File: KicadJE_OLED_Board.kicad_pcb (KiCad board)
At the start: 2 copper layers, 170.6 x 128 mm, 164 parts, among them J1 LED 1-6, J201 OLED, J202 ADC Input, J203 Out2, J204 Out1, J205 OUT1, J206 OUT2, J207 IN1, J208 IN2, J209 CV1, J210 CV2, J211 FrontLED, J212 -12V Front, J301 UART, J302 AVR-ISP-6, P1 Doepfer_Power_16pin, P201 Doepfer_Power_16pin, SW201 Rotary_Encoder_Switch, SW202 Rotary_Encoder_Switch, U201 TL072, U301 ATmega32A-AU, Y301 16MHz

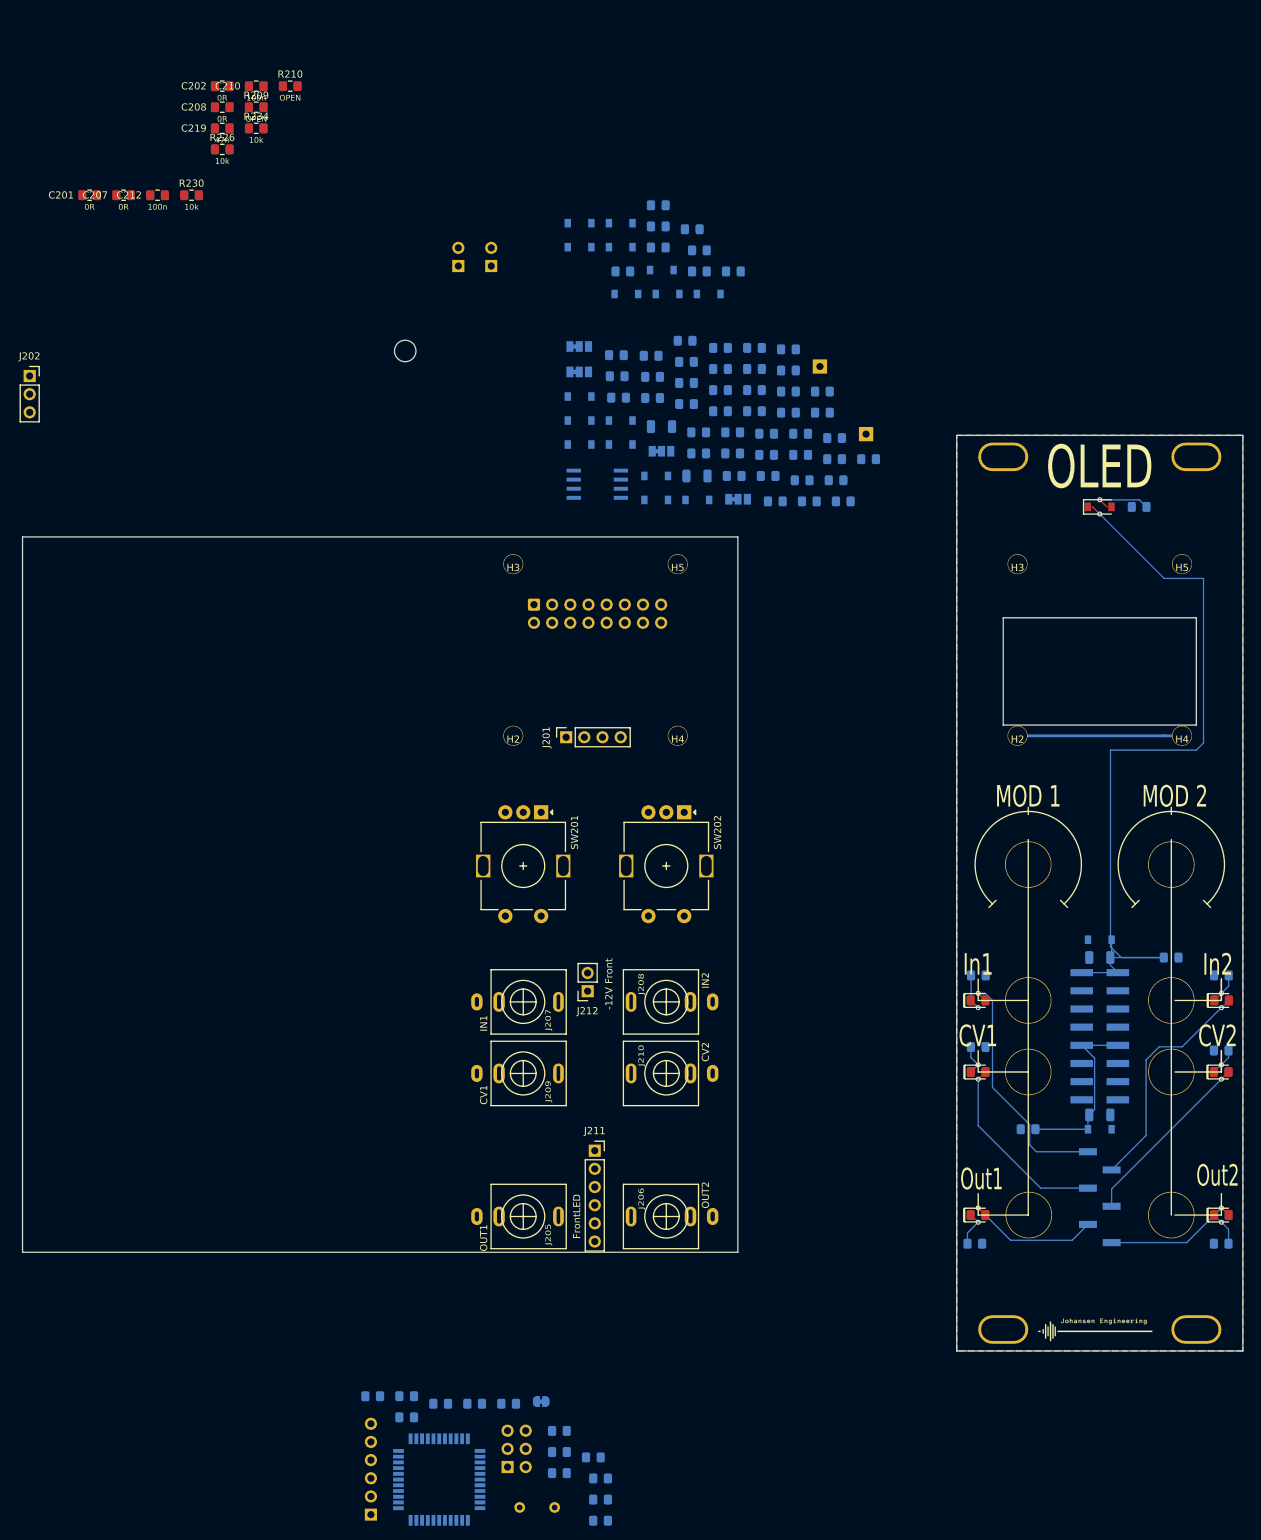
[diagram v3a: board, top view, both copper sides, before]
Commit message: Most components placed
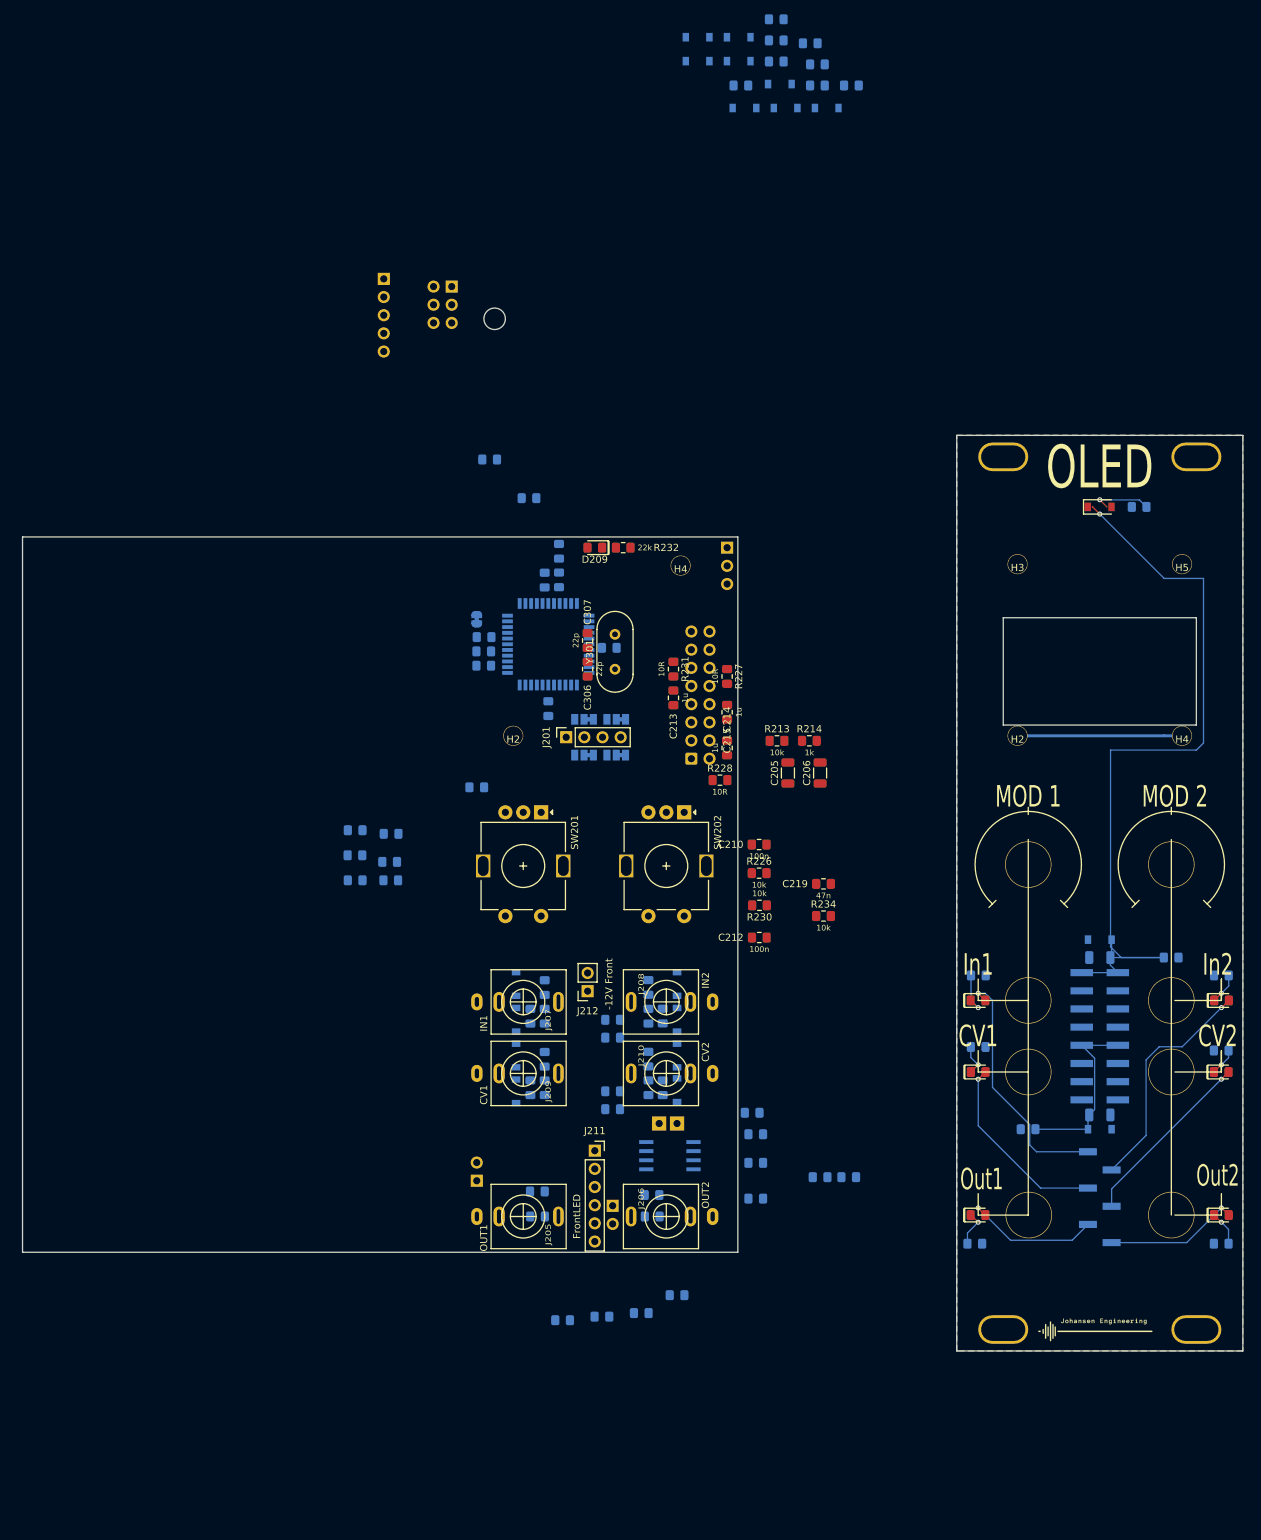
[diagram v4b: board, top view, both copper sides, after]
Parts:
- removed C216, C217: 100n, AJ:C_0805_AJ
- removed the H3 at (168.6, 53.8)
- removed the H5 at (191.6, 53.8)
- C201, C202, C207, C208, J202, R209, R210: moved to B.Cu
- C205, C206, C213, C214, C215, C306, C307, D209, R213, R214, R227, R228, R231, R232, Y301: moved to F.Cu
- J301: footprint Connector_PinHeader_2.54mm:PinHeader_1x06_P2.54mm_Vertical -> Connector_PinHeader_2.54mm:PinHeader_1x05_P2.54mm_Vertical
- moved J301 172.8 mm to (150.5, 13.9), turned to 180 degrees
- moved C208 166.3 mm to (188.0, 145.0), turned to 180 degrees
- moved J302 165.2 mm to (160.0, 15.0), turned to 180 degrees
- moved C207 154.1 mm to (172.0, 145.0)
- moved R210 149.4 mm to (189.5, 127.0), turned to 270 degrees
- moved C202 148.5 mm to (187.5, 123.0), turned to 90 degrees
- moved R209 142.3 mm to (171.0, 127.0), turned to 270 degrees
- moved C305 140.4 mm to (170.8, 44.6)
- moved R305 140.3 mm to (165.3, 39.2)
- moved C201 136.5 mm to (173.0, 123.0), turned to 90 degrees
- moved R234 135.7 mm to (212.0, 103.0)
- moved C219 135.0 mm to (212.0, 98.5)
- moved R215 134.8 mm to (175.5, 159.5)
- moved C212 133.6 mm to (203.0, 106.0)
- moved R219 133.4 mm to (186.5, 158.5)
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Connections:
- net /KicadJE_ADSR_Mega32/ATMega32A.sch/D12_PWM renamed /KicadJE_OLED_Mega32/ATMega32A.sch/D12_PWM
- net /KicadJE_ADSR_Mega32/ATMega32A.sch/D13_PWM renamed /KicadJE_OLED_Mega32/ATMega32A.sch/D13_PWM
- net /KicadJE_ADSR_Mega32/ATMega32A.sch/D14_PWM renamed /KicadJE_OLED_Mega32/ATMega32A.sch/D14_PWM
- net /KicadJE_ADSR_Mega32/ATMega32A.sch/D15_PWM renamed /KicadJE_OLED_Mega32/ATMega32A.sch/D15_PWM
- net /KicadJE_ADSR_Mega32/ATMega32A.sch/D16_SCL renamed /KicadJE_OLED_Mega32/ATMega32A.sch/D16_SCL
- net /KicadJE_ADSR_Mega32/ATMega32A.sch/D17_SDA renamed /KicadJE_OLED_Mega32/ATMega32A.sch/D17_SDA
- net /KicadJE_ADSR_Mega32/ATMega32A.sch/D18 renamed /KicadJE_OLED_Mega32/ATMega32A.sch/D18
- net /KicadJE_ADSR_Mega32/ATMega32A.sch/D19 renamed /KicadJE_OLED_Mega32/ATMega32A.sch/D19
- net /KicadJE_ADSR_Mega32/ATMega32A.sch/D20 renamed /KicadJE_OLED_Mega32/ATMega32A.sch/D20
- net /KicadJE_ADSR_Mega32/ATMega32A.sch/D21 renamed /KicadJE_OLED_Mega32/ATMega32A.sch/D21
- net /KicadJE_ADSR_Mega32/ATMega32A.sch/D22 renamed /KicadJE_OLED_Mega32/ATMega32A.sch/D22
- net /KicadJE_ADSR_Mega32/ATMega32A.sch/D23 renamed /KicadJE_OLED_Mega32/ATMega32A.sch/D23
- net /KicadJE_ADSR_Mega32/ATMega32A.sch/D2_INT2 renamed /KicadJE_OLED_Mega32/ATMega32A.sch/D2_INT2
- net /KicadJE_ADSR_Mega32/ATMega32A.sch/D3_OC0 renamed /KicadJE_OLED_Mega32/ATMega32A.sch/D3_OC0
- net /KicadJE_ADSR_Mega32/ATMega32A.sch/D4 renamed /KicadJE_OLED_Mega32/ATMega32A.sch/D4
- C210 pad 1: 29_A5 -> 11_INT1
- C212 pad 1: 28_A4 -> 10_INT0
- C219 pad 1: 27_A3 -> D1
- R226 pad 1: 29_A5 -> 11_INT1
- R230 pad 2: 28_A4 -> 10_INT0
- R234 pad 1: 27_A3 -> D1
- SW202 pad A: 28_A4 -> 10_INT0
- SW202 pad B: 29_A5 -> 11_INT1
- U301 pad 11: /KicadJE_ADSR_Mega32/ATMega32A.sch/D10_INT0 -> 10_INT0
- U301 pad 12: /KicadJE_ADSR_Mega32/ATMega32A.sch/D11_INT1 -> 11_INT1
- U301 pad 41: /KicadJE_ADSR_Mega32/ATMega32A.sch/D1 -> D1

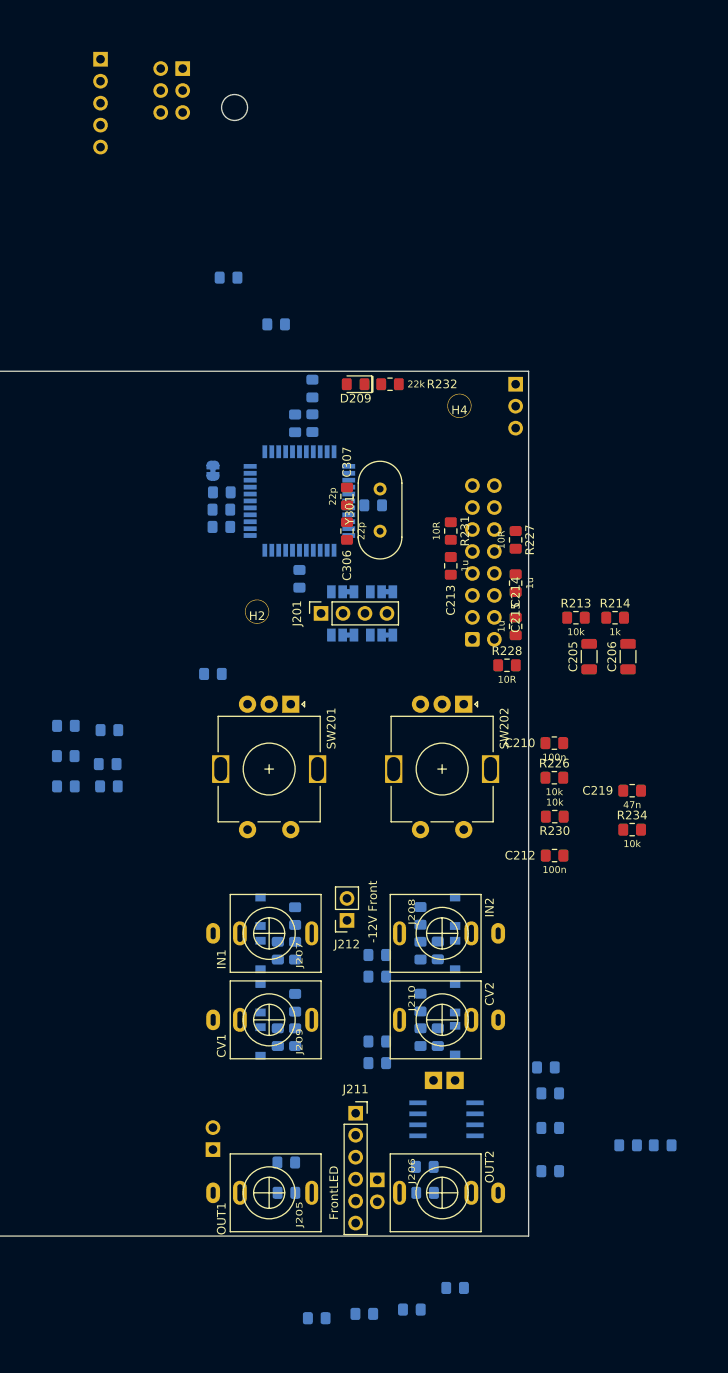
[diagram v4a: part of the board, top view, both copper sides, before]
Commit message: Components placed for KicadJE_OLED_Mega32
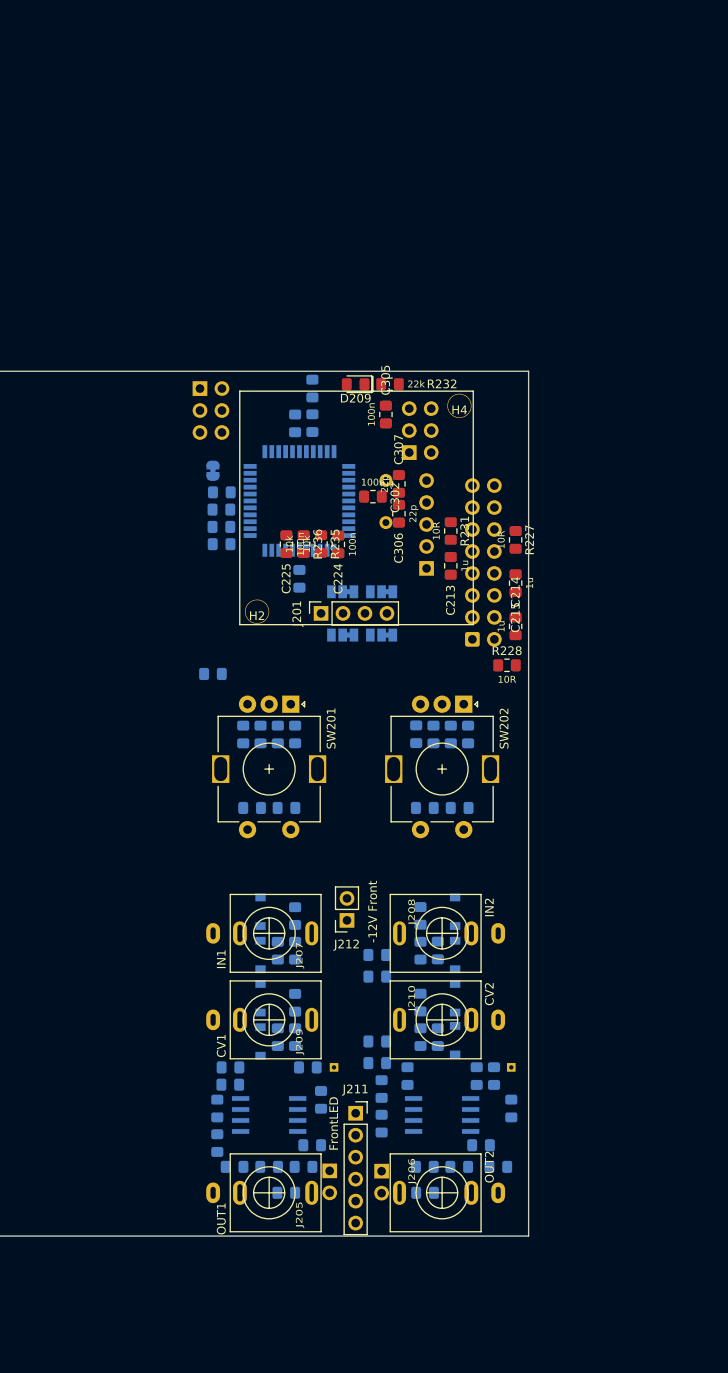
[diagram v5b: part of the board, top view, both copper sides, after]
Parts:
- removed H101: ON, AJ:LED_Hole_3mm
- added C216: 100n, AJ:C_0805_AJ, B.Cu at (183.0, 137.0)
- added C217: 100n, AJ:C_0805_AJ, B.Cu at (164.0, 139.2)
- added C222: 100n, AJ:C_0805_AJ, B.Cu at (175.0, 139.5)
- added C223: 100n, AJ:C_0805_AJ, B.Cu at (165.5, 132.5)
- added C224: 100n, AJ:C_0805_AJ, F.Cu at (178.0, 70.0)
- added C225: 100n, AJ:C_0805_AJ, F.Cu at (172.0, 70.0)
- added R235: 10k, AJ:R_0805_AJ, F.Cu at (176.0, 70.0)
- added R236: 10k, AJ:R_0805_AJ, F.Cu at (174.0, 70.0)
- added U202: TL072, AJ:AJ_SO-8_5.3x6.2mm_P1.27mm, B.Cu at (190.0, 136.0)
- C205: value 1u -> 100n; footprint Capacitor_SMD:C_1206_3216Metric -> AJ:C_0805_AJ; moved to B.Cu
- C206: footprint Capacitor_SMD:C_1206_3216Metric -> AJ:C_0805_AJ; moved to B.Cu
- C210, C212, C219, R213, R226, R230, R234, Y301: moved to B.Cu
- C302, C305: moved to F.Cu
- J202: footprint Connector_PinSocket_2.54mm:PinSocket_1x03_P2.54mm_Vertical -> Connector_PinSocket_2.54mm:PinSocket_2x03_P2.54mm_Vertical
- R214: value 1k -> 10k; moved to B.Cu
- R215, R216, R217, R218, R221: value 20k -> 100k
- R219: value 1k -> 10k
- R220: value 1k -> 100k
- R222: value 20k -> 10k
- TP201, TP202: footprint TestPoint:TestPoint_THTPad_2.0x2.0mm_Drill1.0mm -> TestPoint:TestPoint_THTPad_1.0x1.0mm_Drill0.5mm
- moved C206 70.6 mm to (164.0, 135.2)
- moved J301 69.9 mm to (188.2, 72.8), turned to 0 degrees
- moved R214 65.3 mm to (176.0, 134.2), turned to 90 degrees
- moved R213 57.2 mm to (198.0, 135.2), turned to 90 degrees
- moved J302 51.6 mm to (186.2, 59.4), turned to 0 degrees
- moved C205 49.7 mm to (196.0, 131.5)
- moved J202 36.5 mm to (162.0, 52.0)
- moved R305 30.8 mm to (164.5, 70.0), turned to 180 degrees
- moved R215 30.7 mm to (165.5, 130.5), turned to 180 degrees
- moved C221 30.6 mm to (186.0, 131.5), turned to 270 degrees
- moved R219 30.5 mm to (174.5, 130.5), turned to 180 degrees
- moved C211 24.5 mm to (171.0, 92.0), turned to 90 degrees
- moved R234 24.1 mm to (188.0, 100.5), turned to 180 degrees
- moved C209 23.3 mm to (169.0, 92.0), turned to 90 degrees
- moved R216 22.4 mm to (174.0, 142.0)
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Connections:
- C205 pad 1: GNDA -> Net-(C205-Pad1)
- C205 pad 2: Flow2_32 -> GNDA
- C206 pad 1: GNDA -> Net-(C206-Pad1)
- C206 pad 2: Flow1_32 -> GNDA
- J202 pad 2: 31_A7 -> 27_A3
- R213 pad 1: /KicadJE_OLED_Mega32/ATMega32A.sch/D15_PWM -> Net-(R213-Pad1)
- R213 pad 2: Flow2_32 -> Net-(C216-Pad1)
- R214 pad 1: /KicadJE_OLED_Mega32/ATMega32A.sch/D14_PWM -> Net-(R214-Pad1)
- R214 pad 2: Flow1_32 -> Net-(C217-Pad1)
- R215 pad 1: Flow1_32 -> Net-(C206-Pad1)
- R217 pad 1: Flow2_32 -> Net-(C205-Pad1)
- R219 pad 1: Net-(R219-Pad1) -> Net-(C217-Pad1)
- R219 pad 2: Net-(R216-Pad1) -> Net-(C206-Pad1)
- R220 pad 1: Net-(R220-Pad1) -> Net-(C216-Pad2)
- R221 pad 1: Net-(R219-Pad1) -> Net-(R216-Pad1)
- R222 pad 1: Net-(R220-Pad1) -> Net-(C216-Pad1)
- R222 pad 2: Net-(R222-Pad2) -> Net-(C205-Pad1)
- R224 pad 2: Net-(R222-Pad2) -> Net-(C216-Pad2)
- TP201 pad 1: Flow1_32 -> Net-(C217-Pad1)
- TP202 pad 1: Flow2_32 -> Net-(C216-Pad1)
- U201 pad 3: Flow1_32 -> Net-(C206-Pad1)
- U201 pad 5: Flow2_32 -> Net-(C224-Pad1)
- U201 pad 6: Net-(R218-Pad1) -> Net-(R214-Pad1)
- U201 pad 7: Net-(R222-Pad2) -> Net-(R214-Pad1)
- U301 pad 15: /KicadJE_OLED_Mega32/ATMega32A.sch/D14_PWM -> Flow1_32
- U301 pad 16: /KicadJE_OLED_Mega32/ATMega32A.sch/D15_PWM -> Flow2_32
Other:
- board text added: "A3"
- board text added: "A4"
- board text added: "A5"

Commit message: Filt/Amp Netlist
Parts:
- removed D108, D109, D110, D111: 1N1007, AJ:D_SOD-123
- added C101: 100n, AJ:C_0805_AJ, B.Cu at (178.4, 10.0)
- added C102: 100n, AJ:C_0805_AJ, B.Cu at (174.6, 2.87)
- added C103: 0R, AJ:C_0805_AJ, B.Cu at (184.5, 14.4)
- added C104: 100n, AJ:C_0805_AJ, B.Cu at (168.8, -0.48)
- added C105: 100n, AJ:C_0805_AJ, B.Cu at (192.1, -8.48)
- added C106: 100n, AJ:C_0805_AJ, B.Cu at (196.9, -8.48)
- added H101: ON, AJ:LED_Hole_3mm, F.Cu at (169.7, 21.4)
- added J101: Out1, Connector_PinSocket_2.54mm:PinSocket_1x02_P2.54mm_Vertical, B.Cu at (164.2, 2.57)
- added J102: IN1, AJ:PJ301SM, F.Cu at (150.1, 125.0)
- added J103: OUT1, AJ:PJ301SM, F.Cu at (150.1, 135.0)
- added J104: Out1, Connector_PinSocket_2.54mm:PinSocket_1x02_P2.54mm_Vertical, B.Cu at (173.8, 9.17)
- added J105: IN1, AJ:PJ301SM, F.Cu at (150.1, 115.0)
- added J106: OUT1, AJ:PJ301SM, F.Cu at (150.1, 144.9)
- added P101: Doepfer_Power_10pin, Connector_IDC:IDC-Header_2x05_P2.54mm_Vertical, B.Cu at (149.2, 69.5)
- added R110: 10R, AJ:R_0805_AJ, B.Cu at (175.3, -3.43)
- added R111: 100k, AJ:R_0805_AJ, B.Cu at (187.9, 11.5)
- added R112: 0R, AJ:R_0805_AJ, B.Cu at (179.3, 4.12)
- added R113: 1k, AJ:R_0805_AJ, B.Cu at (165.8, -6.68)
- added R114: 9k1, AJ:R_0805_AJ, B.Cu at (183.2, 7.07)
- added R115: 1k, AJ:R_0805_AJ, B.Cu at (189.3, 14.4)
- added R116: 100k, AJ:R_0805_AJ, B.Cu at (173.6, -0.48)
- added R117: 100k, AJ:R_0805_AJ, B.Cu at (170.6, -3.43)
- added R118: 1k, AJ:R_0805_AJ, B.Cu at (183.2, 10.0)
- added TP101: Flow1, TestPoint:TestPoint_THTPad_1.0x1.0mm_Drill0.5mm, B.Cu at (189.4, 17.7)
- added U101: TL072, AJ:AJ_SO-8_5.3x6.2mm_P1.27mm, B.Cu at (176.8, 15.4)
- D104, D105, D106, D107: footprint AJ:D_SOD-123 -> Diode_SMD:D_SOD-123
- R102, R108, R109: value 10k -> 10R
- R103: value 10k -> 9k1
- R104: value 10k -> 1k
- R106, R107: value 10k -> 100k
- moved R103 41.6 mm to (165.8, -3.73)
- moved D106 41.3 mm to (160.6, -4.53)
- moved R109 39.2 mm to (179.3, 1.17)
- moved R104 37.2 mm to (170.6, -6.38)
- moved R106 37.1 mm to (175.3, -6.38)
- moved D105 35.9 mm to (160.6, -7.88)
- moved R108 35.4 mm to (187.9, 8.52)
- moved D107 35.0 mm to (185.0, 17.6)
- moved D104 34.0 mm to (169.3, 2.67)
- moved R107 34.0 mm to (184.1, 4.12)
- moved R105 33.1 mm to (180.1, -1.78)
- moved R102 29.9 mm to (178.4, 7.07)
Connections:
- D101 pad 1: +12VA -> /InPos
- D102 pad 2: -12VA -> /InNeg
- D105 pad 1: +12VA -> Net-(D104-Pad2)
- D105 pad 2: Net-(D105-Pad2) -> -12VA
- D107 pad 1: +12VA -> Net-(D106-Pad2)
- D107 pad 2: Net-(D107-Pad2) -> -12VA
- R102 pad 1: Net-(D104-Pad2) -> GNDA
- R103 pad 1: Net-(D105-Pad2) -> In1_Filt
- R103 pad 2: Net-(R103-Pad2) -> Net-(D104-Pad2)
- R104 pad 1: Net-(D106-Pad2) -> Net-(D104-Pad2)
- R104 pad 2: Net-(R104-Pad2) -> Net-(C101-Pad1)
- R105 pad 1: Net-(D107-Pad2) -> Net-(C101-Pad1)
- R105 pad 2: Net-(R105-Pad2) -> Net-(C102-Pad1)
- R106 pad 1: Net-(R106-Pad1) -> Net-(C102-Pad1)
- R106 pad 2: Net-(D104-Pad2) -> GNDA
- R107 pad 2: Net-(D105-Pad2) -> GNDA
- R108 pad 1: Net-(R108-Pad1) -> /InPos
- R108 pad 2: Net-(D106-Pad2) -> +12VA
- R109 pad 1: Net-(R109-Pad1) -> /InNeg
- R109 pad 2: Net-(D107-Pad2) -> -12VA
